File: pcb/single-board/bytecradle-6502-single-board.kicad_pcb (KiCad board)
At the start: 2 copper layers, 185.4 x 101.6 mm, 76 parts, among them J1 USB_B, J4 VIA, J8 UART1, SW1 SW_SPDT, SW2 RESET, SW3 NMI, U1 74AC14, U10 74HC273, U11 74HC273, U12 74HC245, U13 74HC245, U14 74AC10, U15 SST39SF040, U16 AS6C4008-55, U17 62256-55, U18 CD74HC688, U19 W65C22NxP, U2 W65C02, U20 CD74HC688, U21 W65C51NxP, U22 MAX232, U3 CD74HC688, U4 74AC08, U5 CD74HC688, U6 CD74HC688, U7 74AC04, U8 74AC10, U9 74AC00, X1 14 MHz, Y1 1.8432 MHz

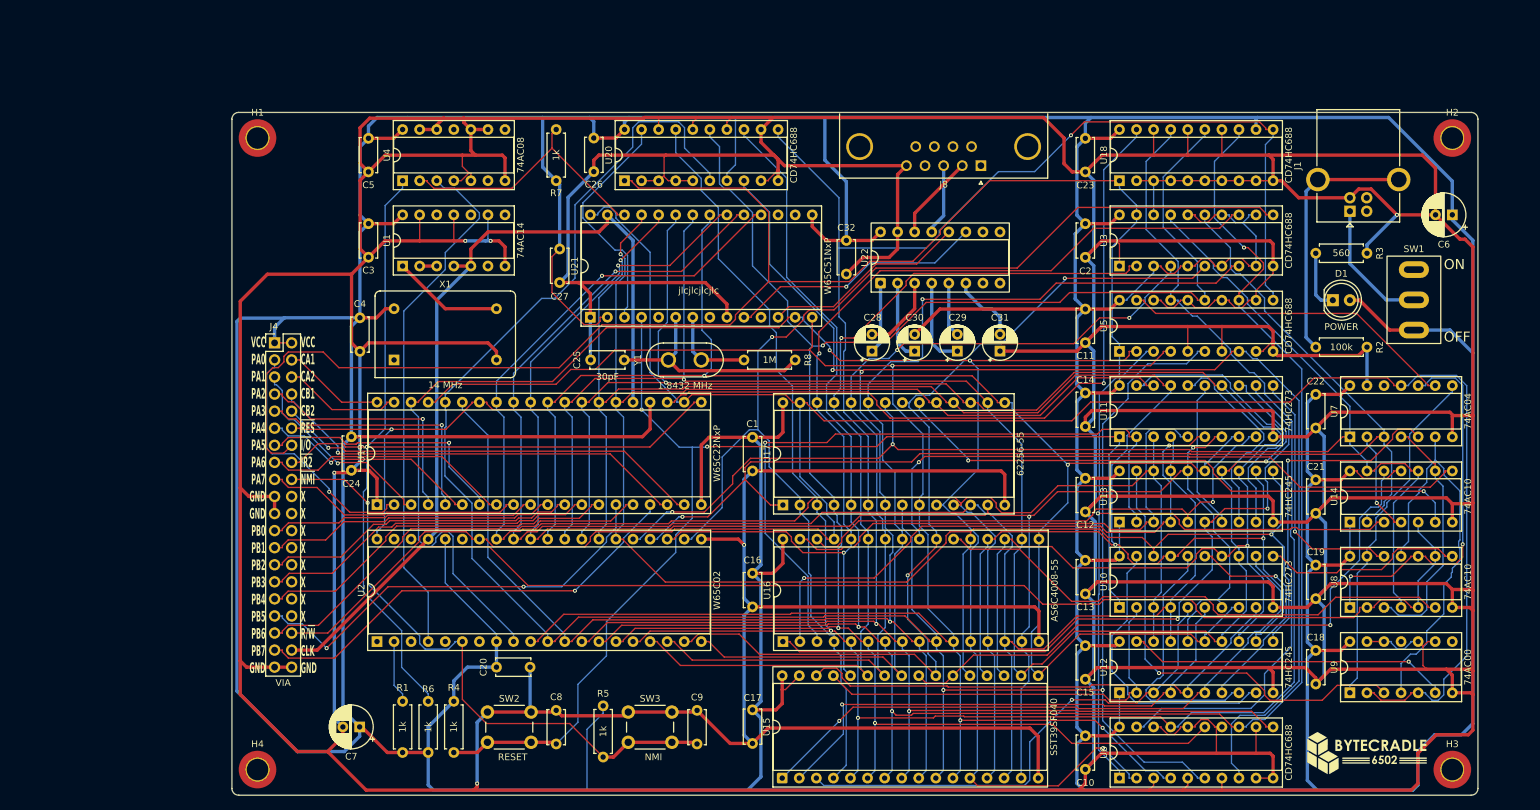
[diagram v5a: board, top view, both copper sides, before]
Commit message: Cleaning repository and completing SD-card reading using bitbang SPI
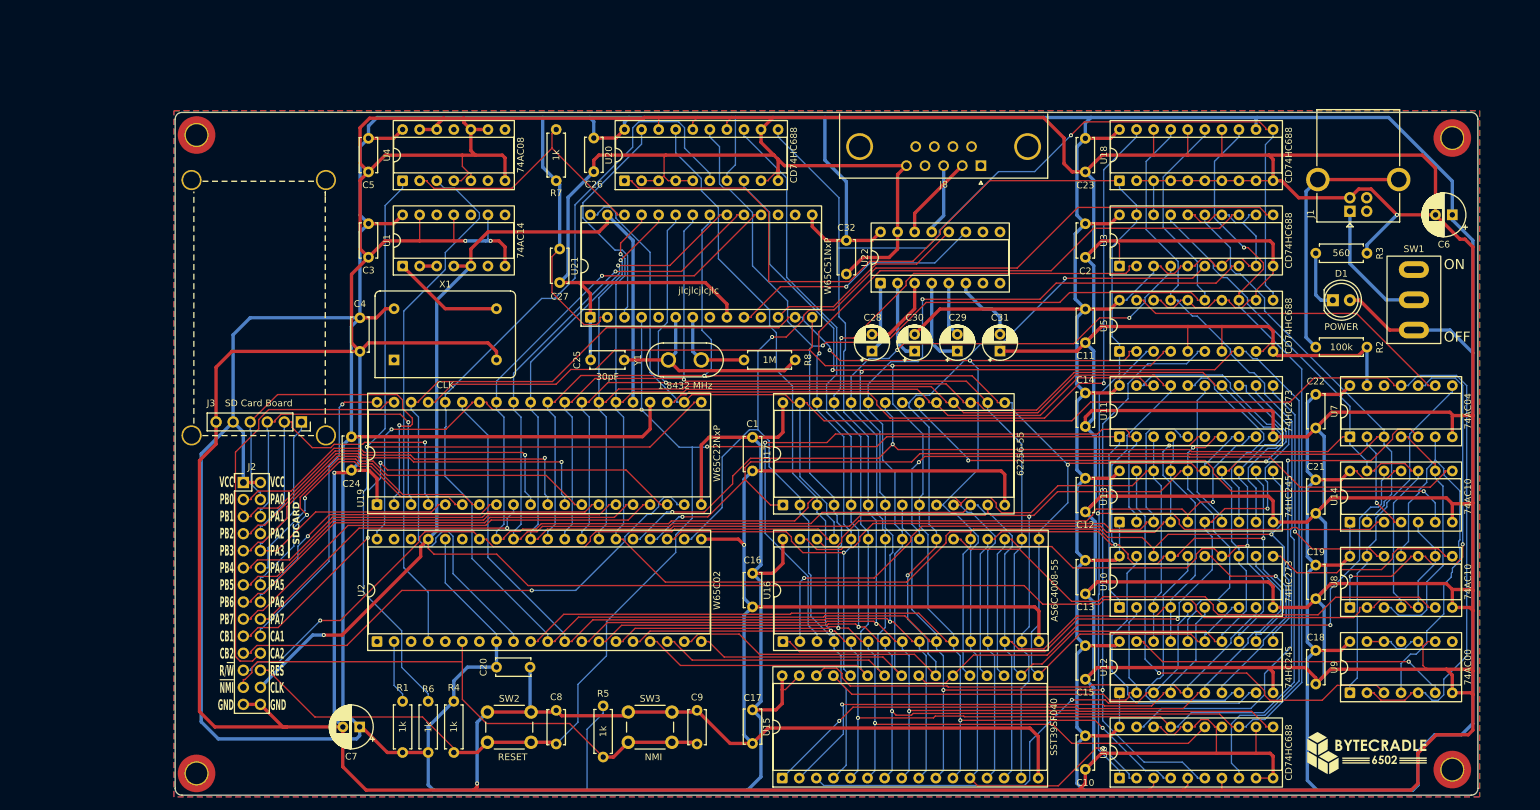
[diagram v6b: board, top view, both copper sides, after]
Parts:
- removed J4: VIA, Connector_PinHeader_2.54mm:PinHeader_2x20_P2.54mm_Vertical
- added J2: Conn_02x14_Odd_Even, Connector_PinHeader_2.54mm:PinHeader_2x14_P2.54mm_Vertical, F.Cu at (81.7, 95.7)
- added J3: SD Card Board, sdcard-holder:sdcard-socket, F.Cu at (90.3, 86.7)
- X1: value 14 MHz -> CLK
- moved H4 9.09 mm to (74.8, 139.0)
- moved H1 9.08 mm to (74.8, 44.0)
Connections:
- U19 pad 2: PA0 -> MISO
- U19 pad 3: PA1 -> MOSI
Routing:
- net ~{I/O}: track 330.8 -> 232.0 mm
- net MISO: track 0.00 -> 55.5 mm, vias 0 -> 1
- net MOSI: track 0.00 -> 49.3 mm, vias 0 -> 1
- net CA2: track 17.8 -> 62.5 mm
- net PA0: track 37.8 -> 0.00 mm, vias 1 -> 0
- net PA1: track 31.4 -> 0.00 mm, vias 1 -> 0
- net CA1: track 15.3 -> 45.0 mm, vias 0 -> 1
- net ~{RES}: track 254.8 -> 274.3 mm
- net CB1: track 64.0 -> 82.0 mm, vias 1 -> 2
- net PA3: track 38.0 -> 52.3 mm, vias 1 -> 0
- net PA2: track 36.8 -> 51.1 mm
- net PB0: track 39.9 -> 53.4 mm, vias 0 -> 1
- net PB1: track 43.5 -> 56.8 mm, vias 0 -> 1
- net VCC: track 1308.3 -> 1321.3 mm
- net ~{IRQC22}: track 149.0 -> 136.5 mm
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- added copper zone on F.Cu, net GND
- added copper zone on B.Cu, net VCC
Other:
- board size 185.4 x 101.6 mm -> 193.9 x 101.6 mm
- board text added: "SDCARD"
- board text added: "VCC PA0 PA1 PA2 PA3 PA4 PA5 PA6 PA7 CA1 CA2 ~{RES} CLK GND"
- board text added: "VCC PB0 PB1 PB2 PB3 PB4 PB5 PB6 PB7 CB1 CB2 R/~{W} ~{NMI} GND"
- board text removed: "VCC CA1 CA2 CB1 CB2 ~{RES} ~{I/O} ~{IR2} ~{NMI} X X X X X X X X R/~{W} CLK GND"
- board text removed: "VCC PA0 PA1 PA2 PA3 PA4 PA5 PA6 PA7 GND GND PB0 PB1 PB2 PB3 PB4 PB5 PB6 PB7 GND"
